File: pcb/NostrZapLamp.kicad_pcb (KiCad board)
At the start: 2 copper layers, 40.6 x 52.1 mm, 5 parts, among them J1 LED, J2 Button, U1 ESP32_DevKit_V1_DOIT

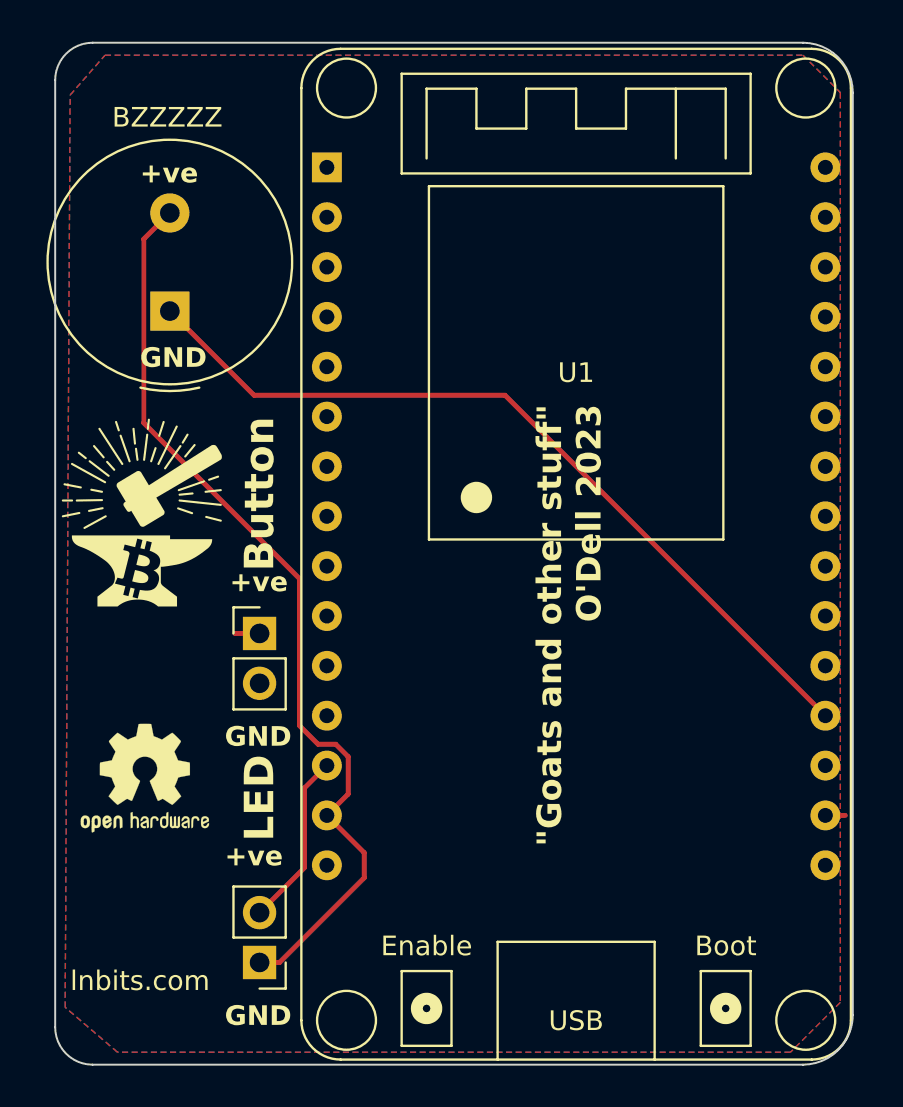
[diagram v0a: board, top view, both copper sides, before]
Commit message: PCB tweaks. Update gitignore to exclude kicad locks
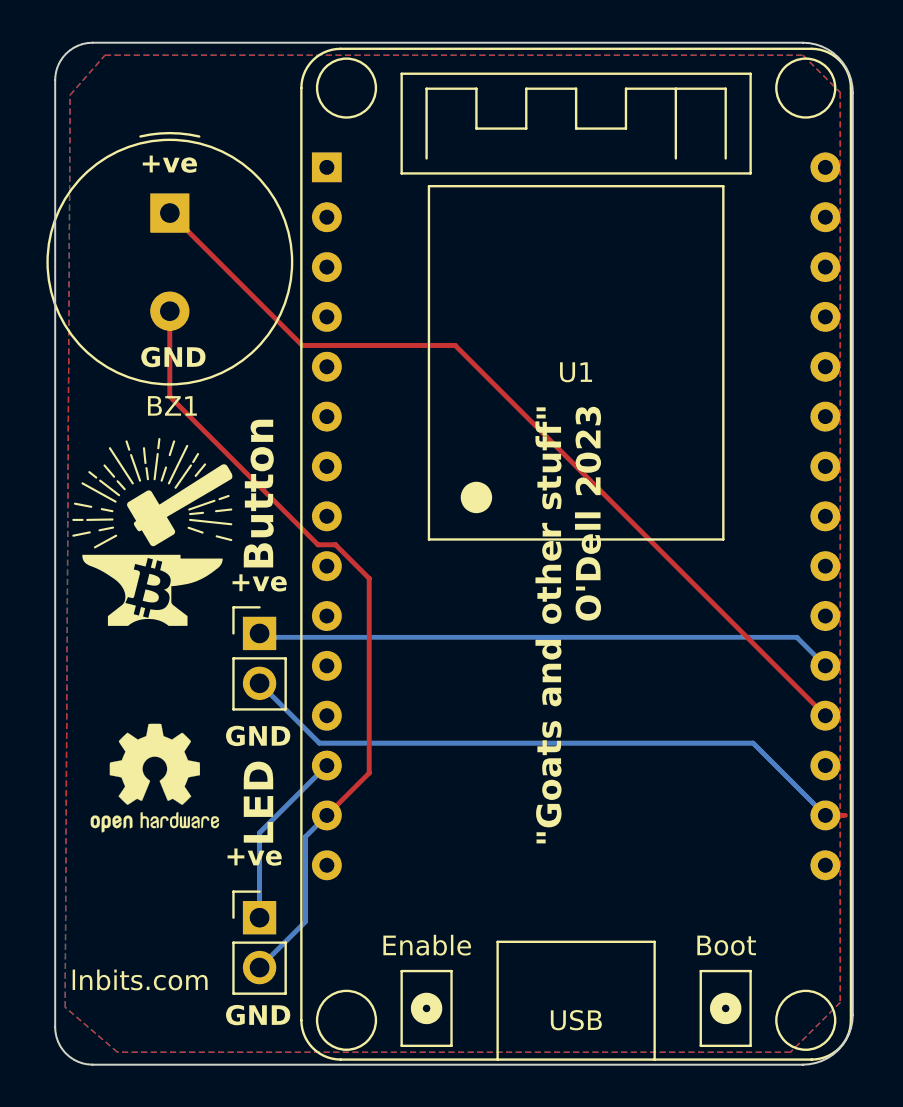
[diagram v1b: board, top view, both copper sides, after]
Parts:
- moved BZ1 5.00 mm to (115.1, 77.9), turned to -90 degrees
- moved J1 2.28 mm to (119.6, 113.8), turned to 0 degrees
- moved REF** 0.51 mm to (114.3, 106.7)
- renumbered BZZZZZ to BZ1
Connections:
- J1 pad 1: Net-(BZ1-+) -> Net-(J1-Pin_1)
- J1 pad 2: Net-(J1-Pin_2) -> Net-(BZ1-+)
- U1 pad 13: Net-(J1-Pin_2) -> Net-(J1-Pin_1)
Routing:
- net Net-(J2-Pin_2): track 1.02 -> 32.6 mm
- net Net-(J2-Pin_1): track 1.27 -> 29.5 mm
- net Net-(J1-Pin_1): track 0.00 -> 9.35 mm
- net Net-(J1-Pin_2): track 9.09 -> 0.00 mm
- net Net-(BZ1-+): track 47.8 -> 40.7 mm
- net Net-(BZ1--): track 41.9 -> 44.0 mm

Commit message: Added quote to PCB
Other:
- board text added: "{dblquote}Nostr is the everything app of freedom{dblquote}"

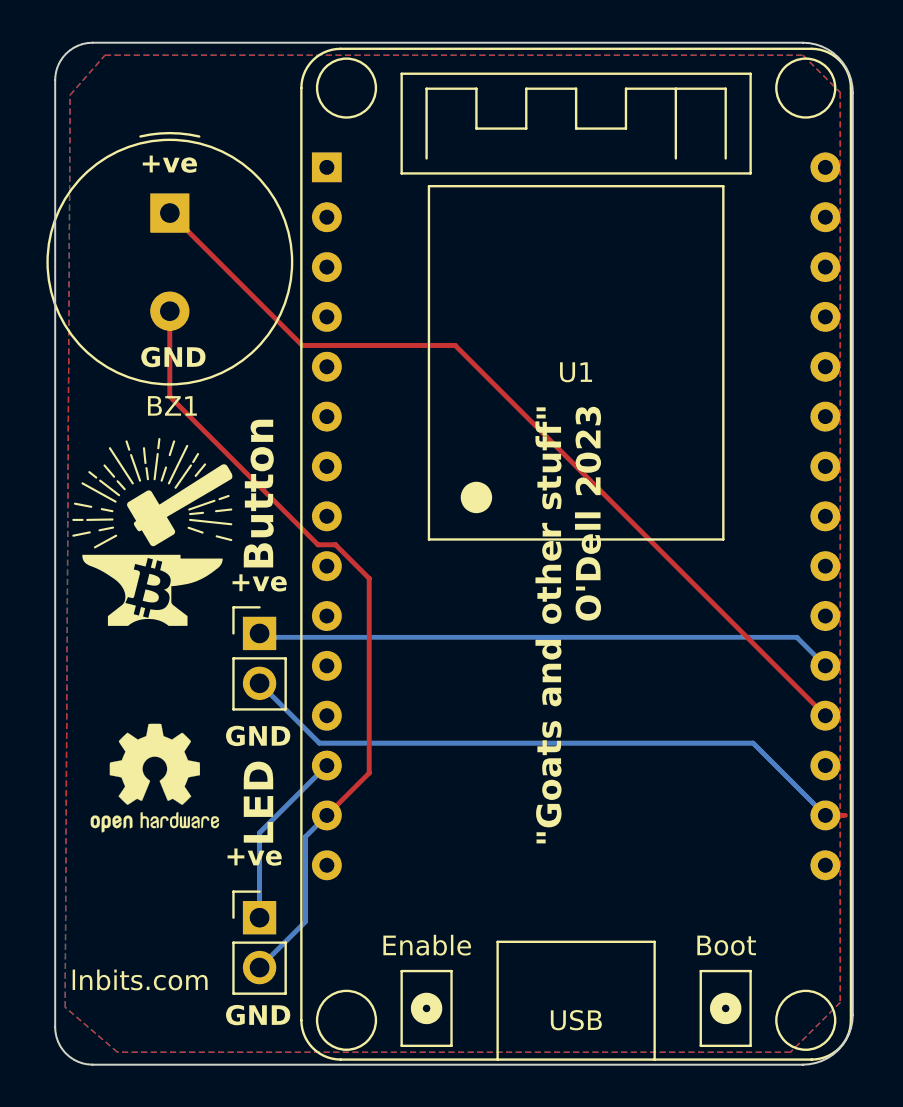
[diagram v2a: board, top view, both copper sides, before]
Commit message: Fixed design rule check issues
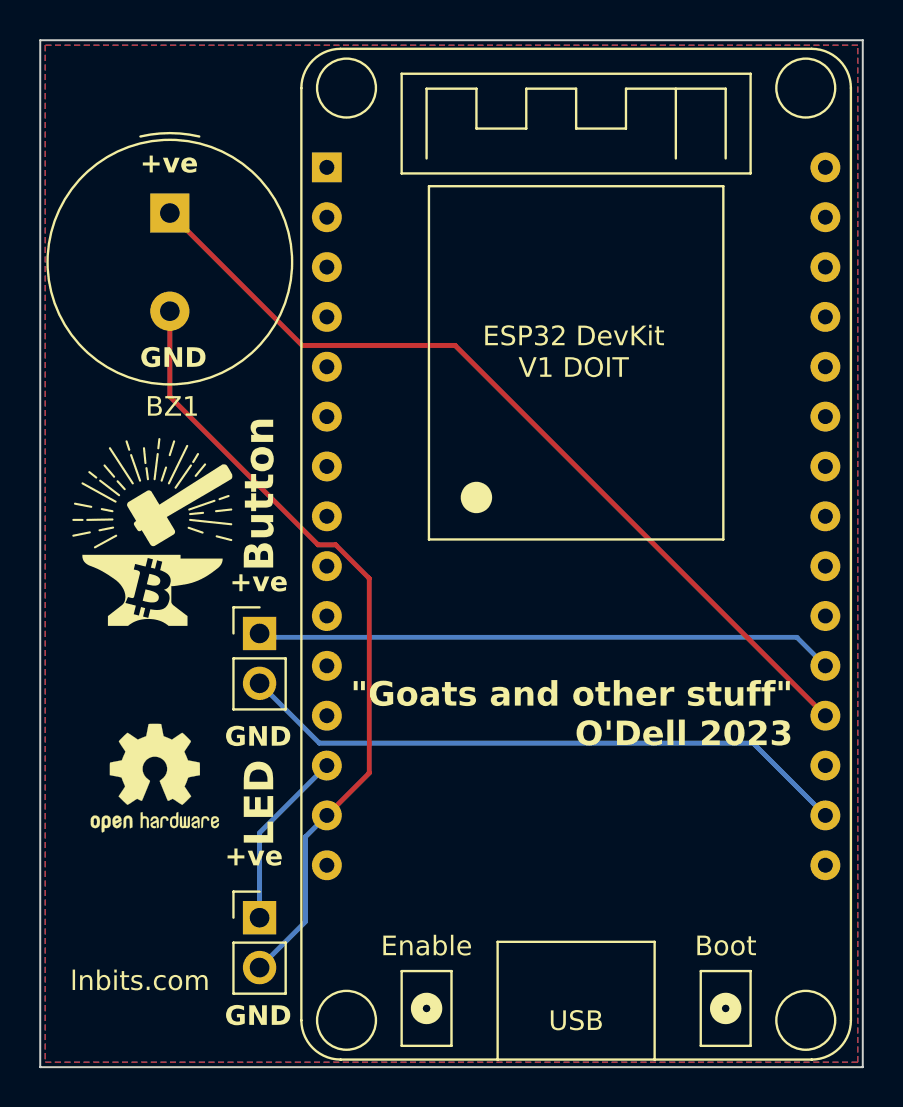
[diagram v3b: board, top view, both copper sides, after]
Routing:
- net Net-(J2-Pin_2): track 32.6 -> 31.6 mm
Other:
- board size 40.6 x 52.1 mm -> 41.9 x 52.3 mm
- board text added: "ESP32 DevKit V1 DOIT"
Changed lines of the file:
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@@
     (property "ki_keywords" "ESP32-WROOM-32 WiFi and Bluetooth microcontroller")
     (attr smd)
-    (fp_text reference "U1" (at 0 10.47) (layer "F.SilkS")
+    (fp_text reference "U1" (at 0 10.47) (layer "F.Fab")
         (effects (font (size 1 1) (thickness 0.15)))
     )
@@
     )
     (stroke (width 0) (type solid)) (fill solid) (layer "F.SilkS"))
-  (gr_line (start 109.22 71.12) (end 109.22 119.38)
-    (stroke (width 0.1) (type default)) (layer "Edge.Cuts"))
-  (gr_line (start 147.32 69.215) (end 111.125 69.215)
-    (stroke (width 0.1) (type default)) (layer "Edge.Cuts"))
-  (gr_arc (start 111.125 121.285) (mid 109.777962 120.727038) (end 109.22 119.38)
-    (stroke (width 0.1) (type default)) (layer "Edge.Cuts"))
-  (gr_line (start 111.125 121.285) (end 147.32 121.285)
-    (stroke (width 0.1) (type default)) (layer "Edge.Cuts"))
-  (gr_arc (start 109.22 71.12) (mid 109.777962 69.772962) (end 111.125 69.215)
-    (stroke (width 0.1) (type default)) (layer "Edge.Cuts"))
-  (gr_line (start 149.86 118.745) (end 149.86 71.755)
-    (stroke (width 0.1) (type default)) (layer "Edge.Cuts"))
-  (gr_arc (start 147.32 69.215) (mid 149.116051 69.958949) (end 149.86 71.755)
-    (stroke (width 0.1) (type default)) (layer "Edge.Cuts"))
-  (gr_arc (start 149.86 118.745) (mid 149.116051 120.541051) (end 147.32 121.285)
-    (stroke (width 0.1) (type default)) (layer "Edge.Cuts"))
+  (gr_rect (start 108.458 69.088) (end 150.368 121.412)
+    (stroke (width 0.1) (type default)) (fill none) (layer "Edge.Cuts"))
   (gr_text "{dblquote}Nostr is the everything\napp of freedom{dblquote}" (at 135.89 96.774) (layer "B.SilkS")
     (effects (font (size 1.25 1.25) (thickness 0.3) bold) (justify bottom mirror))
@@
     (effects (font (size 1 1) (thickness 0.25) bold) (justify left bottom))
   )
-  (gr_text "{dblquote}Goats and other stuff{dblquote}\nO'Dell 2023" (at 137.16 87.63 90) (layer "F.SilkS")
+  (gr_text "{dblquote}Goats and other stuff{dblquote}\nO'Dell 2023" (at 146.812 105.156) (layer "F.SilkS")
     (effects (font (size 1.25 1.25) (thickness 0.3) bold) (justify right bottom))
   )
@@
     (effects (font (size 1 1) (thickness 0.25) bold) (justify left bottom))
   )
+  (gr_text "ESP32 DevKit\nV1 DOIT" (at 135.636 86.36) (layer "F.SilkS")
+    (effects (font (size 1 1) (thickness 0.15)) (justify bottom))
+  )
   (gr_text "GND" (at 113.538 85.852) (layer "F.SilkS")
     (effects (font (size 1 1) (thickness 0.25) bold) (justify left bottom))
@@
     (effects (font (size 1 1) (thickness 0.25) bold) (justify left bottom))
   )
-  (segment (start 122.936 105.918) (end 123.063 106.045) (width 0.25) (layer "F.Cu") (net 1))
   (segment (start 119.634 113.797) (end 119.634 109.474) (width 0.25) (layer "B.Cu") (net 1))
   (segment (start 119.634 109.474) (end 123.063 106.045) (width 0.25) (layer "B.Cu") (net 1))
@@
   (segment (start 119.832 99.512) (end 147.01 99.512) (width 0.25) (layer "B.Cu") (net 2))
   (segment (start 147.01 99.512) (end 148.463 100.965) (width 0.25) (layer "B.Cu") (net 2))
-  (segment (start 149.479 108.585) (end 148.463 108.585) (width 0.25) (layer "F.Cu") (net 3))
   (segment (start 119.634 101.854) (end 122.682 104.902) (width 0.25) (layer "B.Cu") (net 3))
   (segment (start 144.78 104.902) (end 148.463 108.585) (width 0.25) (layer "B.Cu") (net 3))
@@
   (segment (start 129.596 84.638) (end 148.463 103.505) (width 0.25) (layer "F.Cu") (net 29))
   (segment (start 125.222 106.426) (end 123.063 108.585) (width 0.25) (layer "F.Cu") (net 30))
-  (segment (start 122.936 108.458) (end 123.063 108.585) (width 0.25) (layer "F.Cu") (net 30))
   (segment (start 115.062 82.893216) (end 115.062 87.247251) (width 0.25) (layer "F.Cu") (net 30))
   (segment (start 123.513251 94.798) (end 125.222 96.506749) (width 0.25) (layer "F.Cu") (net 30))
@@
     (polygon
       (pts
-        (xy 109.982 71.882)
-        (xy 111.76 69.85)
-        (xy 147.32 69.85)
-        (xy 149.225 71.755)
-        (xy 149.225 118.11)
-        (xy 146.685 120.65)
-        (xy 112.395 120.65)
-        (xy 109.728 118.364)
+        (xy 108.712 69.342)
+        (xy 108.712 121.158)
+        (xy 150.114 121.158)
+        (xy 150.114 69.342)
       )
     )

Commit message: Added arrows for solder points to pcb
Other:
- board text added: "Solder at arrows"
